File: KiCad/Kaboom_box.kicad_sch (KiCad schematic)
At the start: 8 parts, among them P101 HDR-IDC-2_54-2X5P, P102 HDR-IDC-2_54-2X5P, P103 HDR-IDC-2_54-2X5P, P104 HDR-IDC-2_54-2X5P, P105 HDR-IDC-2_54-2X5P, P106 HDR-IDC-2_54-2X5P

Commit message: Layout wip
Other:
- sheet Bottom ports: added SPI_CSn_BOT, SPI_RX_BOT, SPI_SCK_BOT, SPI_TX_BOT; removed SPI0_CSn, SPI0_RX, SPI0_SCK, SPI0_TX
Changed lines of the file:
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@@
-      (effects (font (size 1.27 1.27)) (justify left))
-    )
-    (pin "SPI0_TX" input (at 195.58 118.11 180)
       (effects (font (size 1.27 1.27)) (justify left))
     )
@@
       (effects (font (size 1.27 1.27)) (justify left))
     )
-    (pin "SPI0_SCK" input (at 195.58 115.57 180)
+    (pin "SPI_CSn_BOT" input (at 195.58 113.03 180)
       (effects (font (size 1.27 1.27)) (justify left))
     )
-    (pin "SPI0_CSn" input (at 195.58 113.03 180)
+    (pin "SPI_RX_BOT" input (at 195.58 110.49 180)
       (effects (font (size 1.27 1.27)) (justify left))
     )
-    (pin "SPI0_RX" input (at 195.58 110.49 180)
+    (pin "SPI_SCK_BOT" input (at 195.58 115.57 180)
       (effects (font (size 1.27 1.27)) (justify left))
     )
+    (pin "SPI_TX_BOT" input (at 195.58 118.11 180)
+      (effects (font (size 1.27 1.27)) (justify left))
+    )

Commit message: Ready for review
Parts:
- B101, B102: footprint kikit:Board -> PCM_kikit:Board
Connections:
- net Bottom/+3.3V: now also P106.10; no longer P106.1
- net Bottom/GND: now also P106.1, P106.3, P106.5, P106.7, P106.9; no longer P106.10, P106.2, P106.4, P106.6, P106.8
- net SPI0_CSn_BOT: now also P106.6; no longer P106.5
- net SPI0_CSn_LID: now also P105.6; no longer P105.5
- net SPI0_RX_BOT: now also P106.8; no longer P106.3
- net SPI0_RX_LID: now also P105.8; no longer P105.3
- net SPI0_SCK_BOT: now also P106.4; no longer P106.7
- net SPI0_SCK_LID: now also P105.4; no longer P105.7
- net SPI0_TX_BOT: now also P106.2; no longer P106.9
- net SPI0_TX_LID: now also P105.2; no longer P105.9
- net Top/GND: now also P105.1, P105.3, P105.5, P105.7, P105.9; no longer P105.10, P105.2, P105.4, P105.6, P105.8
- net Top/+3.3V renamed Top/+3.3V_OLED
- net Top/+3.3V_OLED: no longer P105.1
- new net Top/+3.3V_SHIFT: P105.10
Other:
- sheet Top ports: added +3.3V_OLED, +3.3V_SHIFT; removed +3.3V
- moved on the sheet: B101, B102, P105
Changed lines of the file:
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@@
   (junction (at 134.62 87.63) (diameter 0) (color 0 0 0 0)
   )
-  (junction (at 99.06 107.95) (diameter 0) (color 0 0 0 0)
-  )
   (junction (at 134.62 82.55) (diameter 0) (color 0 0 0 0)
   )
@@
     (stroke (width 0) (type default))
   )
-  (wire (pts (xy 99.06 132.08) (xy 91.44 132.08))
-    (stroke (width 0) (type default))
-  )
   (wire (pts (xy 96.52 129.54) (xy 96.52 53.34))
     (stroke (width 0) (type default))
@@
     (stroke (width 0) (type default))
   )
-  (wire (pts (xy 99.06 107.95) (xy 99.06 132.08))
-    (stroke (width 0) (type default))
-  )
   (wire (pts (xy 104.14 87.63) (xy 115.57 87.63))
     (stroke (width 0) (type default))
@@
     (stroke (width 0) (type default))
   )
-  (wire (pts (xy 99.06 107.95) (xy 99.06 80.01))
-    (stroke (width 0) (type default))
-  )
   (wire (pts (xy 130.81 55.88) (xy 134.62 55.88))
     (stroke (width 0) (type default))
@@
     (stroke (width 0) (type default))
   )
-  (wire (pts (xy 99.06 107.95) (xy 115.57 107.95))
+  (wire (pts (xy 91.44 107.95) (xy 115.57 107.95))
     (stroke (width 0) (type default))
   )
@@
     (stroke (width 0) (type default))
   )
-  (wire (pts (xy 99.06 80.01) (xy 115.57 80.01))
+  (wire (pts (xy 91.44 80.01) (xy 115.57 80.01))
     (stroke (width 0) (type default))
   )
@@
     )
   )
-  (symbol (lib_id "HDR-IDC-2_54-2X5P:HDR-IDC-2_54-2X5P") (at 123.19 113.03 0) (unit 1)
-    (in_bom yes) (on_board yes) (dnp no) (fields_autoplaced)
-    (property "Reference" "P105" (at 123.19 100.33 0)
-      (effects (font (size 1.27 1.27)))
-    )
-    (property "Value" "HDR-IDC-2_54-2X5P" (at 123.19 102.87 0)
-      (effects (font (size 1.27 1.27)))
-    )
-    (property "Footprint" "footprint:IDC-TH_10P-P2.54_C5665" (at 123.19 123.19 0)
+  (symbol (lib_id "HDR-IDC-2_54-2X5P:HDR-IDC-2_54-2X5P") (at 123.19 113.03 180) (unit 1)
+    (in_bom yes) (on_board yes) (dnp no)
+    (property "Reference" "P105" (at 123.19 125.73 0)
+      (effects (font (size 1.27 1.27)))
+    )
+    (property "Value" "HDR-IDC-2_54-2X5P" (at 123.19 123.19 0)
+      (effects (font (size 1.27 1.27)))
+    )
+    (property "Footprint" "footprint:IDC-TH_10P-P2.54_C5665" (at 123.19 102.87 0)
       (effects (font (size 1.27 1.27) italic) hide)
     )
-    (property "Datasheet" "https://item.szlcsc.com/6118.html" (at 120.904 112.903 0)
+    (property "Datasheet" "https://item.szlcsc.com/6118.html" (at 125.476 113.157 0)
       (effects (font (size 1.27 1.27)) (justify left) hide)
     )
@@
     )
   )
-  (symbol (lib_id "PCM_kikit:Board") (at 64.77 39.37 0) (unit 1)
-    (in_bom no) (on_board yes) (dnp no) (fields_autoplaced)
-    (property "Reference" "B102" (at 77.47 36.195 0)
+  (symbol (lib_id "PCM_kikit:Board") (at 91.44 46.99 0) (unit 1)
+    (in_bom no) (on_board yes) (dnp no)
+    (property "Reference" "B102" (at 104.14 43.815 0)
       (effects (font (size 1.27 1.27)) (justify left))
     )
-    (property "Value" "Board" (at 77.47 38.735 0)
+    (property "Value" "Board" (at 104.14 46.355 0)
       (effects (font (size 1.27 1.27)) (justify left))
     )
-    (property "Footprint" "kikit:Board" (at 74.93 38.735 0)
-      (effects (font (size 1.27 1.27)) hide)
-    )
-    (property "Datasheet" "" (at 64.77 39.37 0)
+    (property "Footprint" "PCM_kikit:Board" (at 101.6 46.355 0)
+      (effects (font (size 1.27 1.27)) hide)
+    )
+    (property "Datasheet" "" (at 91.44 46.99 0)
       (effects (font (size 1.27 1.27)) hide)
     )
@@
     )
   )
-  (symbol (lib_id "HDR-IDC-2_54-2X5P:HDR-IDC-2_54-2X5P") (at 165.1 113.03 0) (mirror y) (unit 1)
-    (in_bom yes) (on_board yes) (dnp no) (fields_autoplaced)
-    (property "Reference" "P106" (at 165.1 100.33 0)
-      (effects (font (size 1.27 1.27)))
-    )
-    (property "Value" "HDR-IDC-2_54-2X5P" (at 165.1 102.87 0)
-      (effects (font (size 1.27 1.27)))
-    )
-    (property "Footprint" "footprint:IDC-TH_10P-P2.54_C5665" (at 165.1 123.19 0)
+  (symbol (lib_id "HDR-IDC-2_54-2X5P:HDR-IDC-2_54-2X5P") (at 165.1 113.03 0) (mirror x) (unit 1)
+    (in_bom yes) (on_board yes) (dnp no)
+    (property "Reference" "P106" (at 165.1 125.73 0)
+      (effects (font (size 1.27 1.27)))
+    )
+    (property "Value" "HDR-IDC-2_54-2X5P" (at 165.1 123.19 0)
+      (effects (font (size 1.27 1.27)))
+    )
+    (property "Footprint" "footprint:IDC-TH_10P-P2.54_C5665" (at 165.1 102.87 0)
       (effects (font (size 1.27 1.27) italic) hide)
     )
-    (property "Datasheet" "https://item.szlcsc.com/6118.html" (at 167.386 112.903 0)
+    (property "Datasheet" "https://item.szlcsc.com/6118.html" (at 162.814 113.157 0)
       (effects (font (size 1.27 1.27)) (justify left) hide)
     )
@@
     )
   )
-  (symbol (lib_id "PCM_kikit:Board") (at 208.28 34.29 0) (unit 1)
+  (symbol (lib_id "PCM_kikit:Board") (at 262.89 46.99 0) (unit 1)
     (in_bom no) (on_board yes) (dnp no) (fields_autoplaced)
-    (property "Reference" "B101" (at 220.98 31.115 0)
+    (property "Reference" "B101" (at 275.59 43.815 0)
       (effects (font (size 1.27 1.27)) (justify left))
     )
-    (property "Value" "Board" (at 220.98 33.655 0)
+    (property "Value" "Board" (at 275.59 46.355 0)
       (effects (font (size 1.27 1.27)) (justify left))
     )
-    (property "Footprint" "kikit:Board" (at 218.44 33.655 0)
-      (effects (font (size 1.27 1.27)) hide)
-    )
-    (property "Datasheet" "" (at 208.28 34.29 0)
+    (property "Footprint" "PCM_kikit:Board" (at 273.05 46.355 0)
+      (effects (font (size 1.27 1.27)) hide)
+    )
+    (property "Datasheet" "" (at 262.89 46.99 0)
       (effects (font (size 1.27 1.27)) hide)
     )
@@
       (effects (font (size 1.27 1.27)) (justify right))
     )
-    (pin "+3.3V" input (at 91.44 132.08 0)
-      (effects (font (size 1.27 1.27)) (justify right))
-    )
     (pin "VDD" input (at 91.44 129.54 0)
       (effects (font (size 1.27 1.27)) (justify right))
@@
       (effects (font (size 1.27 1.27)) (justify right))
     )
+    (pin "+3.3V_SHIFT" input (at 91.44 107.95 0)
+      (effects (font (size 1.27 1.27)) (justify right))
+    )
+    (pin "+3.3V_OLED" input (at 91.44 80.01 0)
+      (effects (font (size 1.27 1.27)) (justify right))
+    )

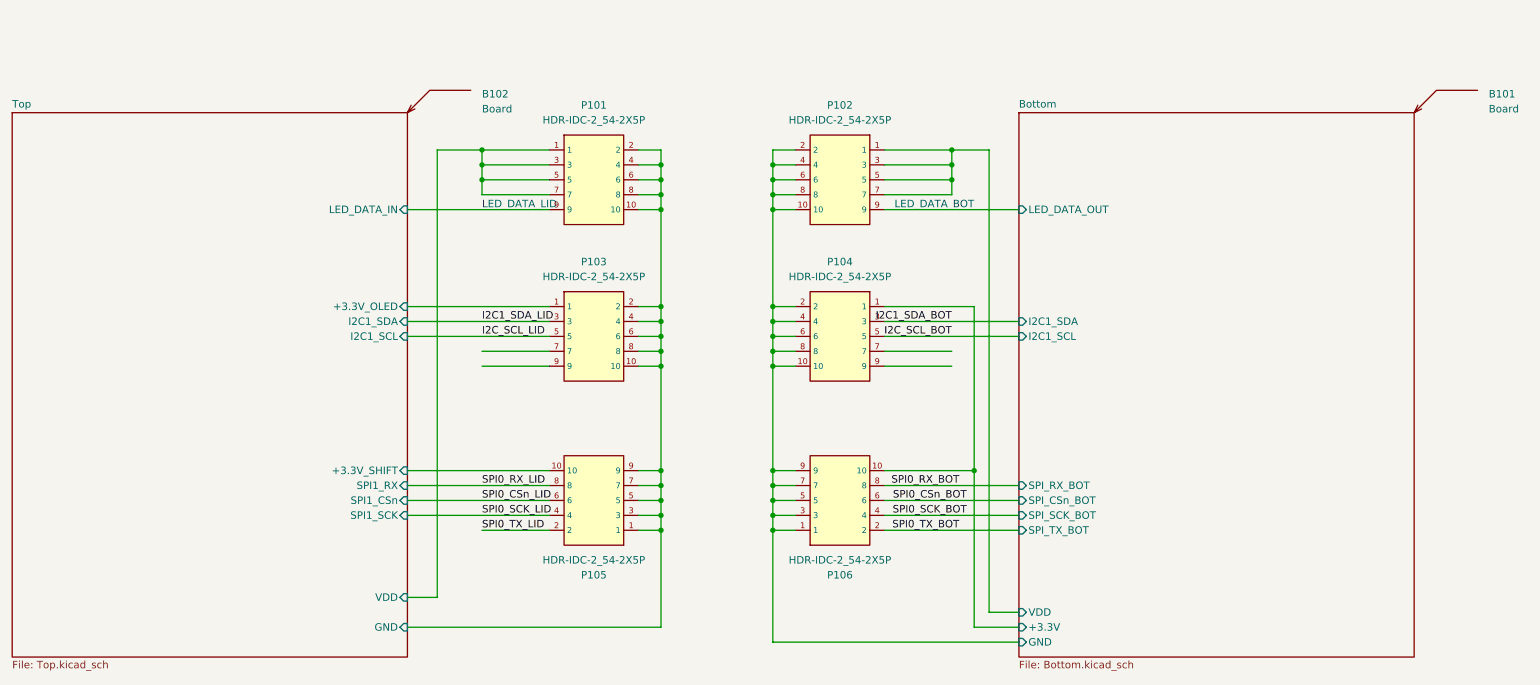
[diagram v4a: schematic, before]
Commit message: Ready for PCB layout with discreet LEDs
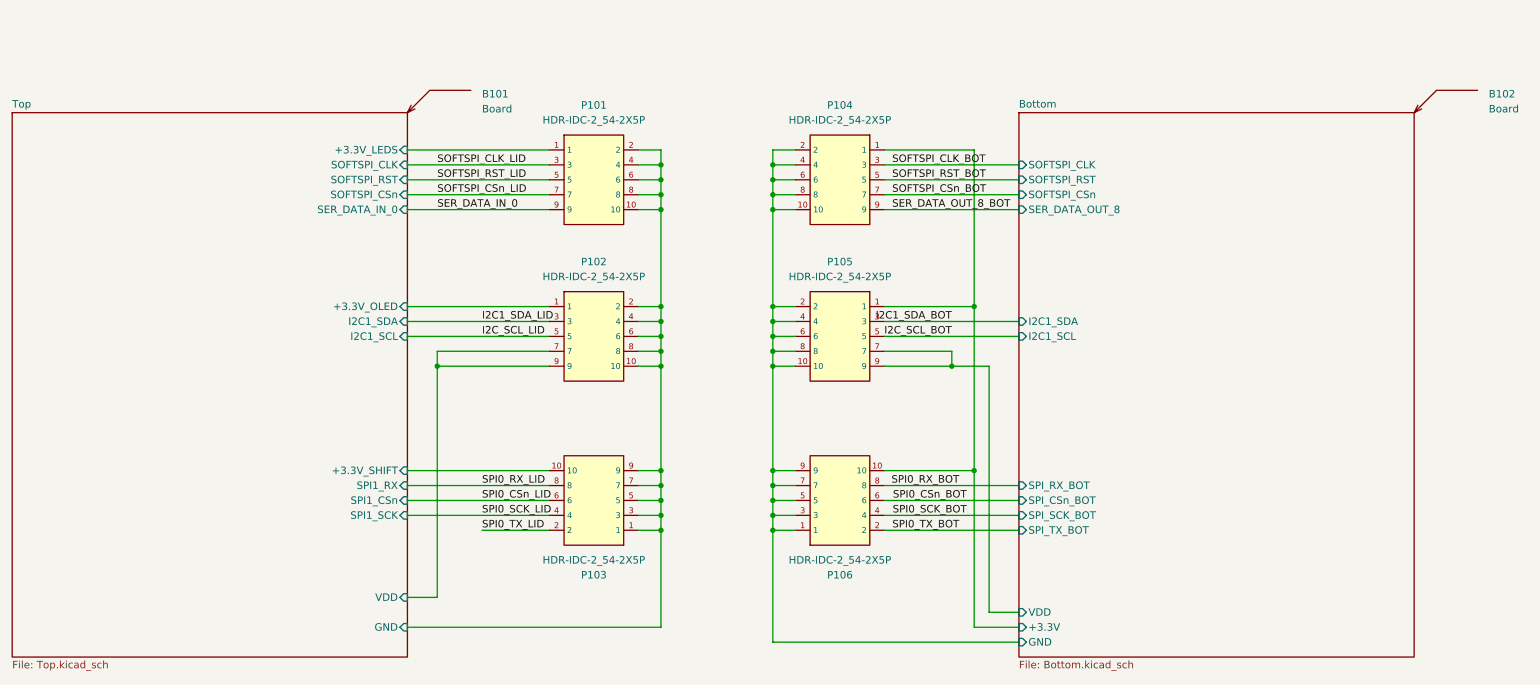
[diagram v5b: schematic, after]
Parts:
- renumbered B102 to B101, B101 to B102, P103 to P102, P105 to P103, P102 to P104, P104 to P105
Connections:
- net Bottom/+3.3V: now also P104.1
- net Bottom/VDD: now also P105.7, P105.9; no longer P104.1, P104.3, P104.5, P104.7
- net Top/VDD: now also P102.7, P102.9; no longer P101.1, P101.3, P101.5, P101.7
- net Bottom/LED_DATA_OUT renamed SER_DATA_OUT_8_BOT
- net Top/LED_DATA_IN renamed SER_DATA_IN_0
- new net SOFTSPI_CLK_BOT: P104.3
- new net SOFTSPI_CLK_LID: P101.3
- new net SOFTSPI_CSn_BOT: P104.7
- new net SOFTSPI_CSn_LID: P101.7
- new net SOFTSPI_RST_BOT: P104.5
- new net SOFTSPI_RST_LID: P101.5
- new net Top/+3.3V_LEDS: P101.1
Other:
- sheet Bottom ports: added SER_DATA_OUT_8, SOFTSPI_CLK, SOFTSPI_CSn, SOFTSPI_RST; removed LED_DATA_OUT
- sheet Top ports: added +3.3V_LEDS, SER_DATA_IN_0, SOFTSPI_CLK, SOFTSPI_CSn, SOFTSPI_RST; removed LED_DATA_IN
- note removed: "LED_DATA_BOT"
- note removed: "LED_DATA_LID"
